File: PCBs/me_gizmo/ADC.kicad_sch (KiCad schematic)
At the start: 28 parts, among them U11 MCP4922, U12 MCP4922, U9 MCP3564R, X4 SG-8018CG_19.6608M-TJHSA3

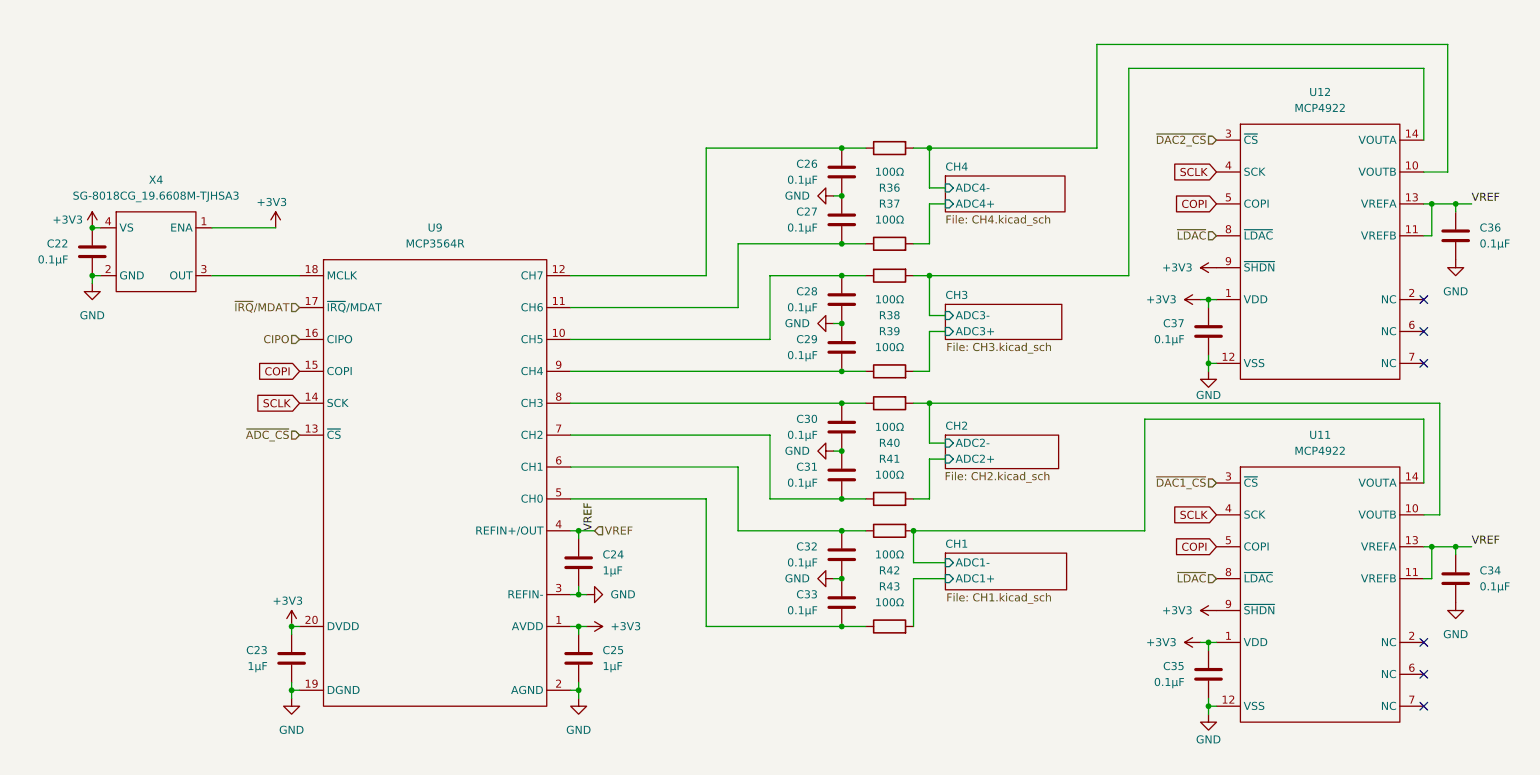
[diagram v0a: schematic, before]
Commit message: Completed first draft of integrated measurement unit
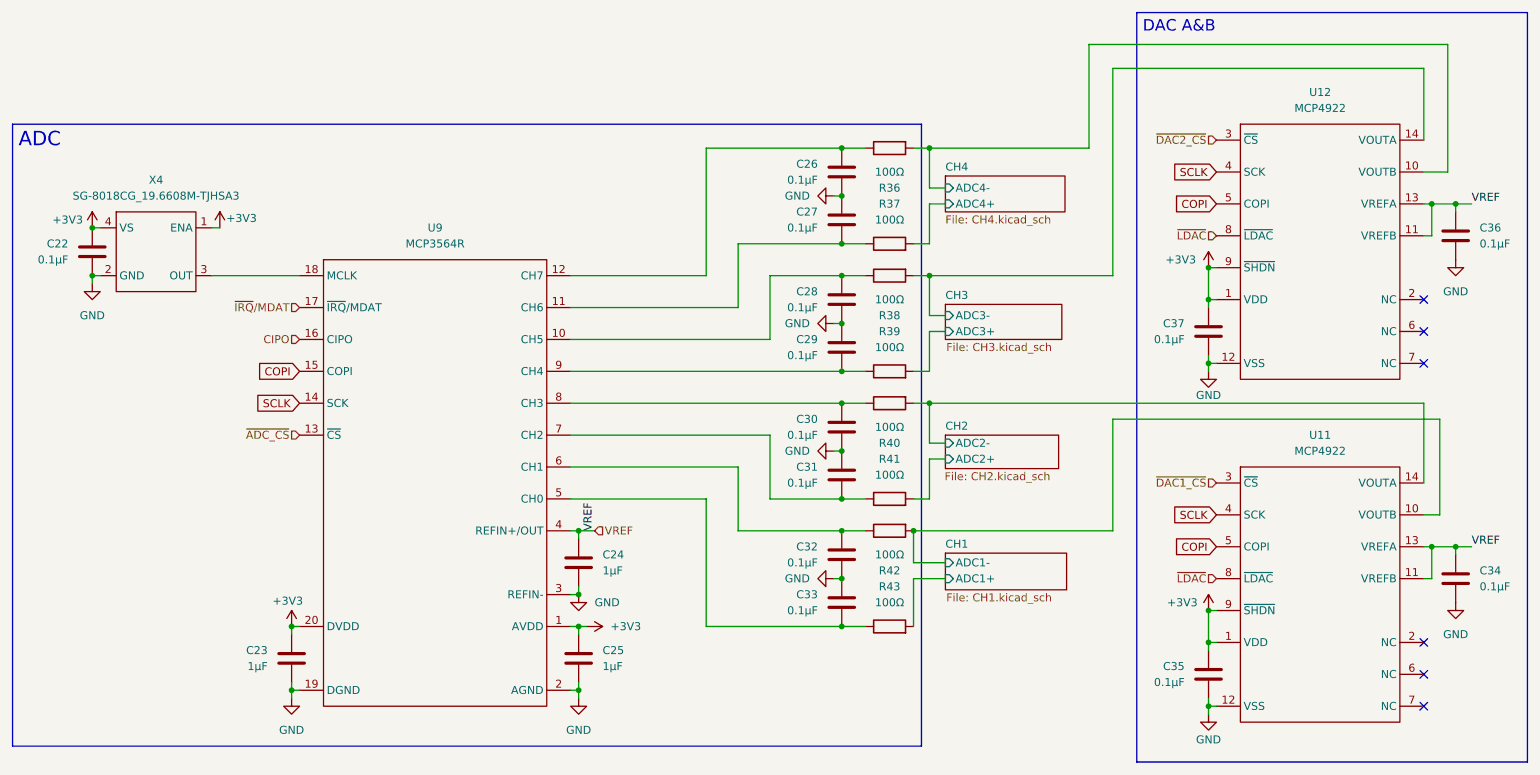
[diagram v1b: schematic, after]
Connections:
- net CH1/ADC1-: now also U11.10 (VOUTB); no longer U11.14 (VOUTA)
- net CH2/ADC2-: now also U11.14 (VOUTA); no longer U11.10 (VOUTB)

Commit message: Switched the DAC connections on channels 3 and 4 to reflect the flipped bridge configurations
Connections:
- net CH3/ADC3+: now also U12.14 (VOUTA)
- net CH3/ADC3-: no longer U12.14 (VOUTA)
- net CH4/ADC4+: now also U12.10 (VOUTB)
- net CH4/ADC4-: no longer U12.10 (VOUTB)
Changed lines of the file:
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@@
+	)
+	(junction
+		(at 172.72 78.74)
+		(diameter 0)
+		(color 0 0 0 0)
 	)
 	(junction
@@
 	)
 	(junction
-		(at 172.72 63.5)
-		(diameter 0)
-		(color 0 0 0 0)
-	)
-	(junction
 		(at 158.75 63.5)
 		(diameter 0)
@@
 	)
 	(junction
-		(at 172.72 43.18)
-		(diameter 0)
-		(color 0 0 0 0)
-	)
-	(junction
 		(at 256.54 106.68)
 		(diameter 0)
@@
 	(junction
 		(at 172.72 83.82)
+		(diameter 0)
+		(color 0 0 0 0)
+	)
+	(junction
+		(at 172.72 58.42)
 		(diameter 0)
 		(color 0 0 0 0)
@@
 	(wire
 		(pts
-			(xy 201.93 63.5) (xy 172.72 63.5)
-		)
-		(stroke
-			(width 0)
-			(type default)
-		)
-	)
-	(wire
-		(pts
 			(xy 142.24 93.98) (xy 115.57 93.98)
 		)
@@
 	(wire
 		(pts
-			(xy 198.12 26.67) (xy 198.12 43.18)
-		)
-		(stroke
-			(width 0)
-			(type default)
-		)
-	)
-	(wire
-		(pts
 			(xy 147.32 99.06) (xy 147.32 88.9)
 		)
@@
 	(wire
 		(pts
+			(xy 172.72 58.42) (xy 198.12 58.42)
+		)
+		(stroke
+			(width 0)
+			(type default)
+		)
+	)
+	(wire
+		(pts
 			(xy 217.17 132.08) (xy 218.44 132.08)
 		)
@@
 	(wire
 		(pts
+			(xy 172.72 78.74) (xy 201.93 78.74)
+		)
+		(stroke
+			(width 0)
+			(type default)
+		)
+	)
+	(wire
+		(pts
 			(xy 115.57 68.58) (xy 142.24 68.58)
 		)
@@
 	(wire
 		(pts
-			(xy 198.12 43.18) (xy 172.72 43.18)
-		)
-		(stroke
-			(width 0)
-			(type default)
-		)
-	)
-	(wire
-		(pts
 			(xy 72.39 119.38) (xy 71.12 119.38)
 		)
@@
 	(wire
 		(pts
-			(xy 201.93 30.48) (xy 201.93 63.5)
+			(xy 201.93 30.48) (xy 201.93 78.74)
 		)
 		(stroke
@@
 		)
 		(stroke
+			(width 0)
+			(type default)
+		)
+	)
+	(wire
+		(pts
+			(xy 198.12 26.67) (xy 198.12 58.42)
+		)
+		(stroke

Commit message: Added Main.py with a channel configuration detection script. Also added a thread that updates the leds to display what the device thinks the current operating mode is, particularly while actively looping detect_config. Finally, there are a bunch of untested updates (mostly software) to make the code compatible with the new board. Any replaced working protoype code exists underneath the revisions labeled with 'protptype above it. This commit contains a few key revisions to the hardware including pulling all of the RGB LEDs to ground so that they can be enabled, and pull down resistors on the adc channels that are not connected to the DAC.
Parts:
- added R60, R61, R62, R63: 100kΩ, Resistor_SMD:R_0603_1608Metric, symbol Device:R
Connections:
- net CH1/ADC1+: now also R62.2
- net CH2/ADC2+: now also R63.2
- net CH3/ADC3-: now also R61.2
- net CH4/ADC4-: now also R60.2
- net GND: now also R60.1, R61.1, R62.1, R63.1
